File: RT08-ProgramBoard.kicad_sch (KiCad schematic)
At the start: 5 parts, among them J1 PWR/Addr, J2 Instruction, J3 Data, J4 Instruction, J5 Data

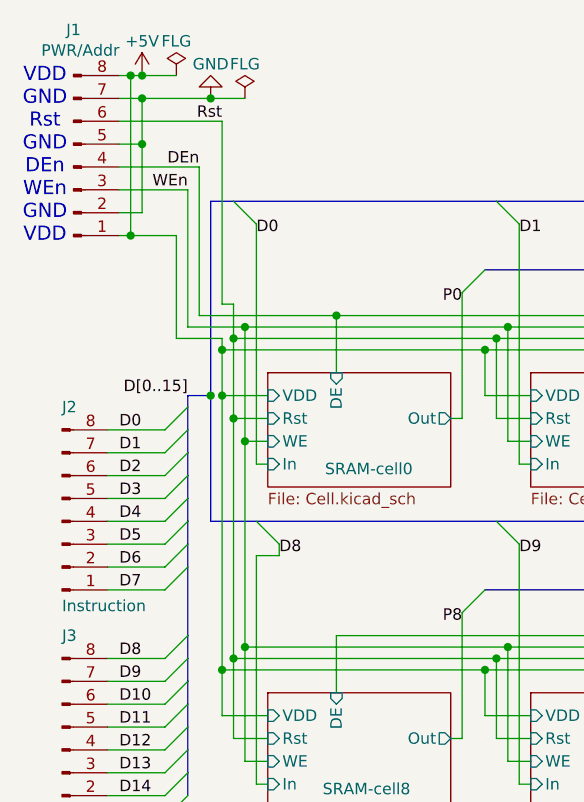
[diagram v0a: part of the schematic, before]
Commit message: Editing Board, VDD and VCC wiring done
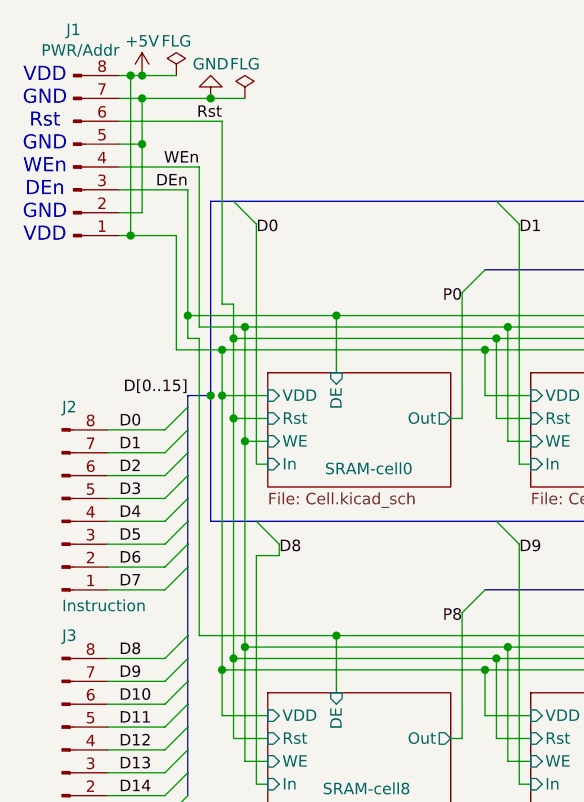
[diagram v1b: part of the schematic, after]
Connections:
- net DEn: now also J1.3 (Pin_3); no longer J1.4 (Pin_4)
- net WEn: now also J1.4 (Pin_4); no longer J1.3 (Pin_3)
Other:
- note added: "VDD GND Rst GND WEn DEn GND VDD"
- note removed: "VDD GND Rst GND DEn WEn GND VDD"
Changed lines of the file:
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@@
 		(comment 4 "This board will be connected to")
 	)
-	(text "VDD\nGND\nRst\nGND\nDEn\nWEn\nGND\nVDD"
+	(text "VDD\nGND\nRst\nGND\nWEn\nDEn\nGND\nVDD"
 		(exclude_from_sim no)
 		(at 14.605 80.01 0)
@@
 	)
 	(junction
-		(at 36.83 99.06)
-		(diameter 0)
-		(color 0 0 0 0)
-	)
-	(junction
 		(at 180.34 137.16)
 		(diameter 0)
@@
 	)
 	(junction
+		(at 30.48 97.79)
+		(diameter 0)
+		(color 0 0 0 0)
+	)
+	(junction
 		(at 66.04 99.06)
 		(diameter 0)
@@
 	)
 	(junction
+		(at 36.83 99.06)
+		(diameter 0)
+		(color 0 0 0 0)
+	)
+	(junction
 		(at 222.25 97.79)
 		(diameter 0)
@@
 	)
 	(junction
+		(at 46.99 133.35)
+		(diameter 0)
+		(color 0 0 0 0)
+	)
+	(junction
 		(at 163.83 97.79)
 		(diameter 0)
@@
 	(wire
 		(pts
+			(xy 30.48 83.82) (xy 30.48 97.79)
+		)
+		(stroke
+			(width 0)
+			(type default)
+		)
+	)
+	(wire
+		(pts
 			(xy 264.16 109.22) (xy 265.43 109.22)
 		)
@@
 	(wire
 		(pts
-			(xy 31.75 97.79) (xy 46.99 97.79)
+			(xy 30.48 97.79) (xy 46.99 97.79)
 		)
 		(stroke
@@
 	(wire
 		(pts
-			(xy 34.29 100.33) (xy 29.21 100.33)
+			(xy 34.29 101.6) (xy 29.21 101.6)
 		)
 		(stroke
@@
 	(wire
 		(pts
+			(xy 31.75 81.28) (xy 31.75 99.06)
+		)
+		(stroke
+			(width 0)
+			(type default)
+		)
+	)
+	(wire
+		(pts
 			(xy 64.77 135.89) (xy 93.98 135.89)
 		)
@@
 		)
 	)
-	(wire
-		(pts
-			(xy 30.48 83.82) (xy 30.48 99.06)
-		)
-		(stroke
-			(width 0)
-			(type default)
-		)
-	)
 	(bus
 		(pts
@@
 	(wire
 		(pts
-			(xy 31.75 81.28) (xy 31.75 97.79)
-		)
-		(stroke
-			(width 0)
-			(type default)
-		)
-	)
-	(wire
-		(pts
 			(xy 134.62 133.35) (xy 163.83 133.35)
 		)
@@
 	(wire
 		(pts
+			(xy 46.99 133.35) (xy 31.75 133.35)
+		)
+		(stroke
+			(width 0)
+			(type default)
+		)
+	)
+	(wire
+		(pts
 			(xy 273.05 118.11) (xy 278.13 118.11)
 		)
@@
 		)
 	)
+	(wire
+		(pts
+			(xy 31.75 99.06) (xy 36.83 99.06)
+		)
+		(stroke
+			(width 0)
+			(type default)
+		)
+	)
 	(bus
 		(pts
@@
 		)
 	)
+	(wire
+		(pts
+			(xy 30.48 97.79) (xy 30.48 100.33)
+		)
+		(stroke
+			(width 0)
+			(type default)
+		)
+	)
 	(bus
 		(pts
@@
 	(wire
 		(pts
-			(xy 34.29 100.33) (xy 34.29 101.6)
-		)
-		(stroke
-			(width 0)
-			(type default)
-		)
-	)
-	(wire
-		(pts
 			(xy 121.92 137.16) (xy 121.92 142.24)
 		)
@@
 	(wire
 		(pts
-			(xy 29.21 100.33) (xy 29.21 88.9)
+			(xy 29.21 101.6) (xy 29.21 88.9)
 		)
 		(stroke
@@
 	(wire
 		(pts
+			(xy 31.75 133.35) (xy 31.75 100.33)
+		)
+		(stroke
+			(width 0)
+			(type default)
+		)
+	)
+	(wire
+		(pts
 			(xy 154.94 149.86) (xy 156.21 149.86)
 		)
@@
 	(wire
 		(pts
+			(xy 30.48 100.33) (xy 31.75 100.33)
+		)
+		(stroke
+			(width 0)
+			(type default)
+		)
+	)
+	(wire
+		(pts
 			(xy 76.2 133.35) (xy 76.2 139.7)
 		)
@@
 		)
 	)
-	(wire
-		(pts
-			(xy 30.48 99.06) (xy 36.83 99.06)
-		)
-		(stroke
-			(width 0)
-			(type default)
-		)
-	)
 	(bus
 		(pts
@@
 		)
 	)
-	(label "WEn"
+	(label "DEn"
 		(at 30.48 83.82 180)
 		(effects
@@
 		)
 	)
-	(label "DEn"
+	(label "WEn"
 		(at 31.75 81.28 180)
 		(effects

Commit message: Editing board, size-optimizing
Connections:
- net DEn: now also J1.4 (Pin_4); no longer J1.3 (Pin_3)
- net WEn: now also J1.3 (Pin_3); no longer J1.4 (Pin_4)
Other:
- note added: "VDD GND Rst GND DEn WEn GND VDD"
- note removed: "VDD GND Rst GND WEn DEn GND VDD"
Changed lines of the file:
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@@
 		(comment 4 "This board will be connected to")
 	)
-	(text "VDD\nGND\nRst\nGND\nWEn\nDEn\nGND\nVDD"
+	(text "VDD\nGND\nRst\nGND\nDEn\nWEn\nGND\nVDD"
 		(exclude_from_sim no)
 		(at 14.605 80.01 0)
@@
 	)
 	(junction
-		(at 30.48 97.79)
-		(diameter 0)
-		(color 0 0 0 0)
-	)
-	(junction
 		(at 66.04 99.06)
 		(diameter 0)
@@
 	)
 	(junction
+		(at 31.75 97.79)
+		(diameter 0)
+		(color 0 0 0 0)
+	)
+	(junction
 		(at 193.04 97.79)
 		(diameter 0)
@@
 	(wire
 		(pts
-			(xy 30.48 83.82) (xy 30.48 97.79)
-		)
-		(stroke
-			(width 0)
-			(type default)
-		)
-	)
-	(wire
-		(pts
 			(xy 264.16 109.22) (xy 265.43 109.22)
 		)
@@
 	(wire
 		(pts
-			(xy 30.48 97.79) (xy 46.99 97.79)
-		)
-		(stroke
-			(width 0)
-			(type default)
-		)
-	)
-	(wire
-		(pts
 			(xy 242.57 123.19) (xy 242.57 149.86)
 		)
@@
 	(wire
 		(pts
-			(xy 31.75 81.28) (xy 31.75 99.06)
-		)
-		(stroke
-			(width 0)
-			(type default)
-		)
-	)
-	(wire
-		(pts
 			(xy 64.77 135.89) (xy 93.98 135.89)
 		)
@@
 	(wire
 		(pts
+			(xy 31.75 97.79) (xy 46.99 97.79)
+		)
+		(stroke
+			(width 0)
+			(type default)
+		)
+	)
+	(wire
+		(pts
 			(xy 35.56 109.22) (xy 39.37 109.22)
 		)
@@
 	(wire
 		(pts
-			(xy 31.75 99.06) (xy 36.83 99.06)
+			(xy 30.48 99.06) (xy 36.83 99.06)
 		)
 		(stroke
@@
 		)
 	)
+	(wire
+		(pts
+			(xy 31.75 81.28) (xy 31.75 97.79)
+		)
+		(stroke
+			(width 0)
+			(type default)
+		)
+	)
 	(bus
 		(pts
@@
 	(wire
 		(pts
-			(xy 30.48 97.79) (xy 30.48 100.33)
+			(xy 31.75 97.79) (xy 31.75 133.35)
 		)
 		(stroke
@@
 	(wire
 		(pts
-			(xy 31.75 133.35) (xy 31.75 100.33)
-		)
-		(stroke
-			(width 0)
-			(type default)
-		)
-	)
-	(wire
-		(pts
 			(xy 154.94 149.86) (xy 156.21 149.86)
 		)
@@
 	(wire
 		(pts
-			(xy 30.48 100.33) (xy 31.75 100.33)
-		)
-		(stroke
-			(width 0)
-			(type default)
-		)
-	)
-	(wire
-		(pts
 			(xy 76.2 133.35) (xy 76.2 139.7)
 		)
@@
 		)
 	)
+	(wire
+		(pts
+			(xy 30.48 83.82) (xy 30.48 99.06)
+		)
+		(stroke
+			(width 0)
+			(type default)
+		)
+	)
 	(bus
 		(pts
@@
 		)
 	)
-	(label "DEn"
-		(at 30.48 83.82 180)
-		(effects
-			(font
-				(size 1.27 1.27)
-			)
-			(justify right bottom)
-		)
-	)
 	(label "P12"
 		(at 276.86 146.05 180)
@@
 		)
 	)
+	(label "WEn"
+		(at 30.48 83.82 180)
+		(effects
+			(font
+				(size 1.27 1.27)
+			)
+			(justify right bottom)
+		)
+	)
 	(label "P14"
 		(at 236.22 132.08 180)
@@
 		)
 	)
+	(label "DEn"
+		(at 31.75 81.28 180)
+		(effects
+			(font
+				(size 1.27 1.27)
+			)
+			(justify right bottom)
+		)
+	)
 	(label "D1"
 		(at 67.31 88.9 0)
@@
 		(effects
 			(font
-				(size 1.27 1.27)
-			)
-			(justify right bottom)
-		)
-	)
-	(label "WEn"
-		(at 31.75 81.28 180)
-		(effects
-			(font

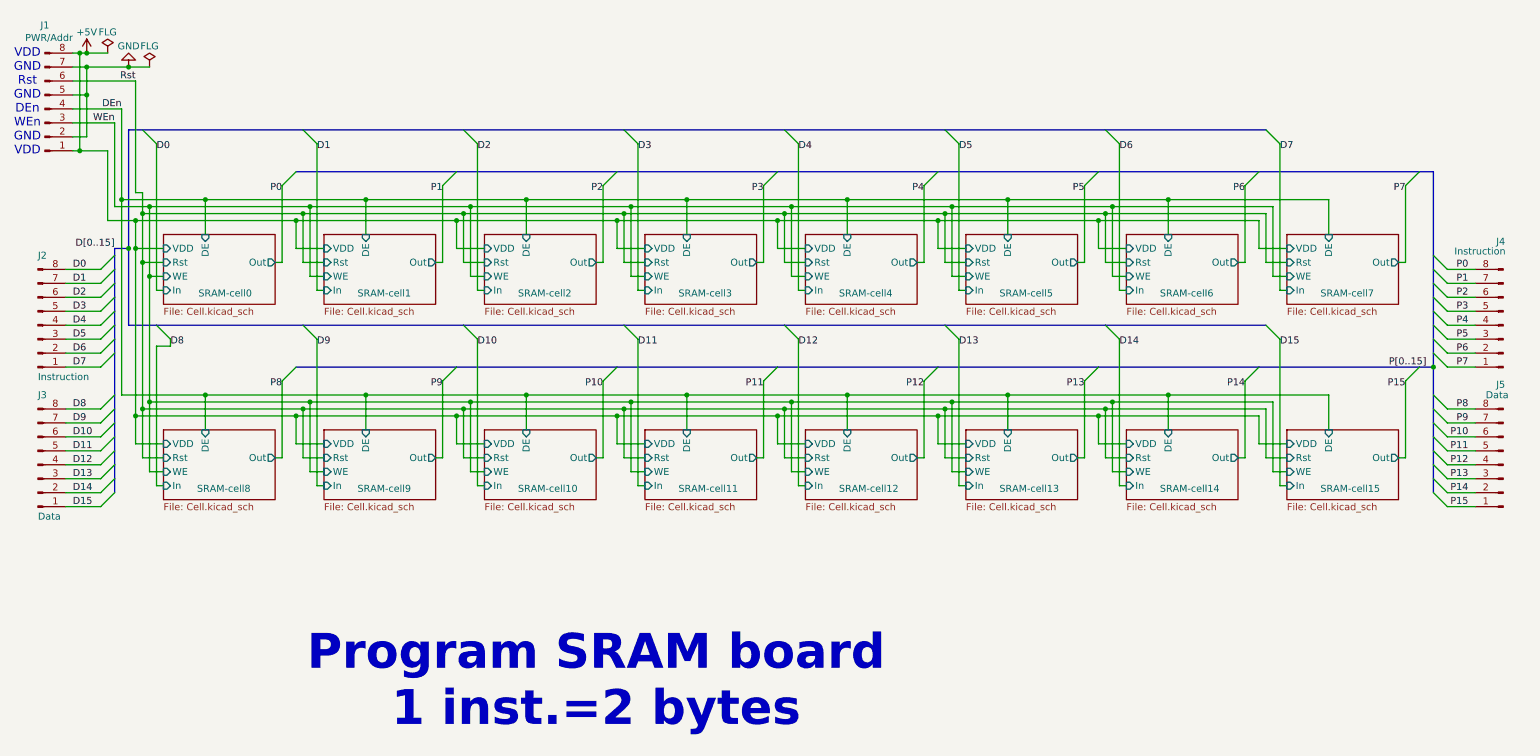
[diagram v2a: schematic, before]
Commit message: Edited pinouts so it can be connected.
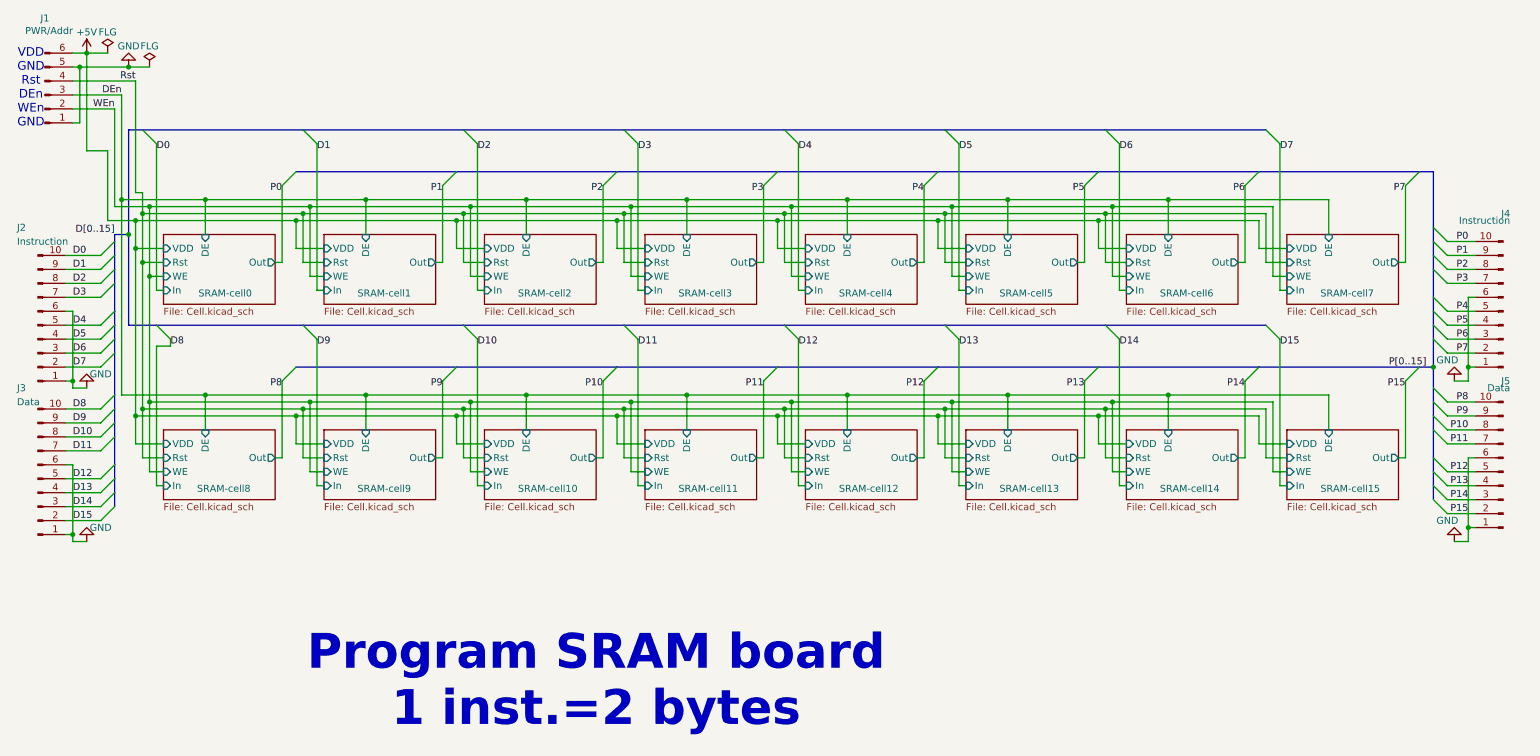
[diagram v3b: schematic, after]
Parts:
- J1: footprint Connector_PinHeader_2.54mm:PinHeader_1x08_P2.54mm_Horizontal -> Connector_PinHeader_2.54mm:PinHeader_1x06_P2.54mm_Horizontal; symbol Connector:Conn_01x08_Pin -> Connector:Conn_01x06_Pin
- J2, J3, J4: footprint Connector_PinHeader_2.54mm:PinHeader_1x08_P2.54mm_Horizontal -> Connector_PinHeader_2.54mm:PinHeader_1x10_P2.54mm_Horizontal; symbol Connector:Conn_01x08_Pin -> Connector:Conn_01x10_Pin
- J5: symbol Connector:Conn_01x08_Pin -> Connector:Conn_01x10_Pin
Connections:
- net D12 is gone; now on net GND: J3.4 (Pin_4)
- net D13 is gone; now on net GND: J3.3 (Pin_3)
- net D14 is gone; now on net GND: J3.2 (Pin_2)
- net D15 is gone; now on net GND: J3.1 (Pin_1)
- net D4 is gone; now on net GND: J2.4 (Pin_4)
- net D5 is gone; now on net GND: J2.3 (Pin_3)
- net D6 is gone; now on net GND: J2.2 (Pin_2)
- net D7 is gone; now on net GND: J2.1 (Pin_1)
- net P12 is gone; now on net GND: J5.4 (Pin_4)
- net P13 is gone; now on net GND: J5.3 (Pin_3)
- net P14 is gone; now on net GND: J5.2 (Pin_2)
- net P15 is gone; now on net GND: J5.1 (Pin_1)
- net P4 is gone; now on net GND: J4.4 (Pin_4)
- net P5 is gone; now on net GND: J4.3 (Pin_3)
- net P6 is gone; now on net GND: J4.2 (Pin_2)
- net P7 is gone; now on net GND: J4.1 (Pin_1)
- net +5V: now also J1.6 (Pin_6); no longer J1.1 (Pin_1), J1.8 (Pin_8)
- net D0: now also J2.10 (Pin_10); no longer J2.8 (Pin_8)
- net D1: now also J2.9 (Pin_9); no longer J2.7 (Pin_7)
- net D10: now also J3.8 (Pin_8); no longer J3.6 (Pin_6)
- net D11: now also J3.7 (Pin_7); no longer J3.5 (Pin_5)
- net D2: now also J2.8 (Pin_8); no longer J2.6 (Pin_6)
- net D3: now also J2.7 (Pin_7); no longer J2.5 (Pin_5)
- net D8: now also J3.10 (Pin_10); no longer J3.8 (Pin_8)
- net D9: now also J3.9 (Pin_9); no longer J3.7 (Pin_7)
- net DEn: now also J1.3 (Pin_3); no longer J1.4 (Pin_4)
- net GND: now also J1.1 (Pin_1), J2.5 (Pin_5), J2.6 (Pin_6), J3.5 (Pin_5), J3.6 (Pin_6), J4.5 (Pin_5), J4.6 (Pin_6), J5.5 (Pin_5), J5.6 (Pin_6); no longer J1.2 (Pin_2), J1.7 (Pin_7)
- net P0: now also J4.10 (Pin_10); no longer J4.8 (Pin_8)
- net P1: now also J4.9 (Pin_9); no longer J4.7 (Pin_7)
- net P10: now also J5.8 (Pin_8); no longer J5.6 (Pin_6)
- net P11: now also J5.7 (Pin_7); no longer J5.5 (Pin_5)
- net P2: now also J4.8 (Pin_8); no longer J4.6 (Pin_6)
- net P3: now also J4.7 (Pin_7); no longer J4.5 (Pin_5)
- net P8: now also J5.10 (Pin_10); no longer J5.8 (Pin_8)
- net P9: now also J5.9 (Pin_9); no longer J5.7 (Pin_7)
- net Rst: now also J1.4 (Pin_4); no longer J1.6 (Pin_6)
- net WEn: now also J1.2 (Pin_2); no longer J1.3 (Pin_3)
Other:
- note added: "VDD GND Rst DEn WEn GND"
- note removed: "VDD GND Rst GND DEn WEn GND VDD"
